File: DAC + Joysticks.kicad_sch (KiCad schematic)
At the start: 131 parts, among them J10 L Phono, J11 R Phono, J8 JOY0, J9 JOY1, U23 74HC374, U24 74HC374, U25 74HC244, U26 74HC244, U27 74HC373, U28 74HC244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

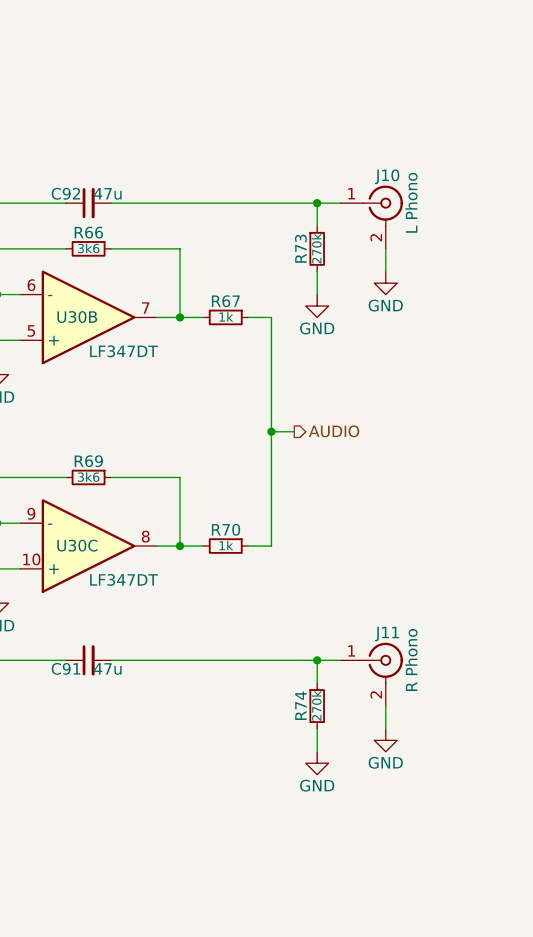
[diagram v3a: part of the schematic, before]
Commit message: motherboard: Added the main RCA-based audio out connections, completing the audio section
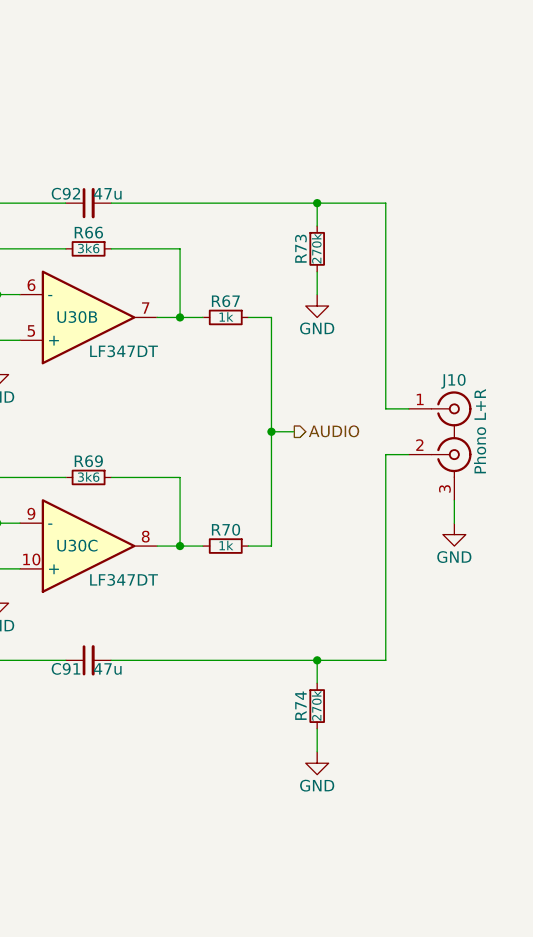
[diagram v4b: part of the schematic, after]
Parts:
- removed J10: L Phono, symbol Connector:Conn_Coaxial
- removed J11: R Phono, symbol Connector:Conn_Coaxial
- added J10: Phono L+R, rhais_connector-multicomp:PSG01550, symbol Connector:Conn_Coaxial_x2
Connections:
- net GND: now also J10.3 (EXT)
- net at C91.2, R74.1: now also J10.2 (IN2)
- net at C92.2, R73.1: now also J10.1 (IN1)
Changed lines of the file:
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@@
 	(wire
 		(pts
+			(xy 393.7 205.74) (xy 396.24 205.74)
+		)
+		(stroke
+			(width 0)
+			(type default)
+		)
+	)
+	(wire
+		(pts
 			(xy 228.6 55.88) (xy 241.3 55.88)
 		)
@@
 	(wire
 		(pts
-			(xy 388.62 177.8) (xy 386.08 177.8)
+			(xy 386.08 177.8) (xy 393.7 177.8)
 		)
 		(stroke
@@
 	(wire
 		(pts
-			(xy 393.7 233.68) (xy 393.7 236.22)
+			(xy 401.32 210.82) (xy 401.32 213.36)
 		)
 		(stroke
@@
 	(wire
 		(pts
-			(xy 393.7 182.88) (xy 393.7 185.42)
-		)
-		(stroke
-			(width 0)
-			(type default)
-		)
-	)
-	(wire
-		(pts
 			(xy 299.72 154.94) (xy 302.26 154.94)
 		)
@@
 	(wire
 		(pts
-			(xy 388.62 228.6) (xy 386.08 228.6)
+			(xy 386.08 228.6) (xy 393.7 228.6)
 		)
 		(stroke
@@
 	(wire
 		(pts
+			(xy 396.24 200.66) (xy 393.7 200.66)
+		)
+		(stroke
+			(width 0)
+			(type default)
+		)
+	)
+	(wire
+		(pts
 			(xy 325.12 142.24) (xy 320.04 142.24)
 		)
@@
 	(wire
 		(pts
+			(xy 393.7 228.6) (xy 393.7 205.74)
+		)
+		(stroke
+			(width 0)
+			(type default)
+		)
+	)
+	(wire
+		(pts
+			(xy 393.7 200.66) (xy 393.7 177.8)
+		)
+		(stroke
+			(width 0)
+			(type default)
+		)
+	)
+	(wire
+		(pts
 			(xy 40.64 81.28) (xy 104.14 81.28)
 		)
@@
 	)
 	(symbol
-		(lib_id "Connector:Conn_Coaxial")
-		(at 393.7 228.6 0)
-		(unit 1)
-		(exclude_from_sim no)
-		(in_bom yes)
-		(on_board yes)
-		(dnp no)
-		(property "Reference" "J11"
-			(at 393.954 225.552 0)
-			(effects
-				(font
-					(size 1.27 1.27)
-				)
-			)
-		)
-		(property "Value" "R Phono"
-			(at 396.621 228.6 90)
-			(effects
-				(font
-					(size 1.27 1.27)
-				)
-			)
-		)
-		(property "Footprint" ""
-			(at 393.7 228.6 0)
-			(effects
-				(font
-					(size 1.27 1.27)
-				)
-				(hide yes)
-			)
-		)
-		(property "Datasheet" "~"
-			(at 393.7 228.6 0)
-			(effects
-				(font
-					(size 1.27 1.27)
-				)
-				(hide yes)
-			)
-		)
-		(property "Description" "coaxial connector (BNC, SMA, SMB, SMC, Cinch/RCA, LEMO, ...)"
-			(at 393.7 228.6 0)
-			(effects
-				(font
-					(size 1.27 1.27)
-				)
-				(hide yes)
-			)
-		)
-		(pin "1"
-		)
-		(pin "2"
-		)
-		(instances
-			(project ""
-				(path "/6cc81c6b-09a2-4492-8ca2-d80a5c796e77/4fddf671-e1bf-4c63-ae08-e5f2b64aff0a"
-					(reference "J11")
-					(unit 1)
-				)
-			)
-		)
-	)
-	(symbol
 		(lib_id "power:GND")
 		(at 350.52 195.58 0)
@@
 	)
 	(symbol
+		(lib_id "Connector:Conn_Coaxial_x2")
+		(at 401.32 203.2 0)
+		(unit 1)
+		(exclude_from_sim no)
+		(in_bom yes)
+		(on_board yes)
+		(dnp no)
+		(property "Reference" "J10"
+			(at 401.32 197.485 0)
+			(effects
+				(font
+					(size 1.27 1.27)
+				)
+			)
+		)
+		(property "Value" "Phono L+R"
+			(at 404.241 203.2 90)
+			(effects
+				(font
+					(size 1.27 1.27)
+				)
+			)
+		)
+		(property "Footprint" "rhais_connector-multicomp:PSG01550"
+			(at 401.32 205.74 0)
+			(effects
+				(font
+					(size 1.27 1.27)
+				)
+				(hide yes)
+			)
+		)
+		(property "Datasheet" "http://www.farnell.com/datasheets/2826737.pdf"
+			(at 401.32 205.74 0)
+			(effects
+				(font
+					(size 1.27 1.27)
+				)
+				(hide yes)
+			)
+		)
+		(property "Description" "double coaxial connector (BNC, SMA, SMB, SMC, Cinch/RCA, LEMO, ...)"
+			(at 401.32 203.2 0)
+			(effects
+				(font
+					(size 1.27 1.27)
+				)
+				(hide yes)
+			)
+		)
+		(property "MFR" "Pro Signal"
+			(at 401.32 203.2 0)
+			(effects
+				(font
+					(size 1.27 1.27)
+				)
+				(hide yes)
+			)
+		)
+		(property "MPN" "PSG01550"
+			(at 401.32 203.2 0)
+			(effects
+				(font
+					(size 1.27 1.27)
+				)
+				(hide yes)
+			)
+		)
+		(property "OC_FARNELL" "1280669"
+			(at 401.32 203.2 0)
+			(effects
+				(font
+					(size 1.27 1.27)
+				)
+				(hide yes)
+			)
+		)
+		(pin "3"
+		)
+		(pin "2"
+		)
+		(pin "1"
+		)
+		(instances
+			(project ""
+				(path "/6cc81c6b-09a2-4492-8ca2-d80a5c796e77/4fddf671-e1bf-4c63-ae08-e5f2b64aff0a"
+					(reference "J10")
+					(unit 1)
+				)
+			)
+		)
+	)
+	(symbol
 		(lib_id "Device:Opamp_Quad")
 		(at 287.02 127 0)
@@
 	(symbol
 		(lib_id "power:GND")
-		(at 393.7 185.42 0)
-		(unit 1)
-		(exclude_from_sim no)
-		(in_bom yes)
-		(on_board yes)
-		(dnp no)
-		(property "Reference" "#PWR0193"
-			(at 393.7 191.77 0)
-			(effects
-				(font
-					(size 1.27 1.27)
-				)
-				(hide yes)
-			)
-		)
-		(property "Value" "GND"
-			(at 393.7 189.23 0)
-			(effects
-				(font
-					(size 1.27 1.27)
-				)
-			)
-		)
-		(property "Footprint" ""
-			(at 393.7 185.42 0)
-			(effects
-				(font
-					(size 1.27 1.27)
-				)
-				(hide yes)
-			)
-		)
-		(property "Datasheet" ""
-			(at 393.7 185.42 0)
-			(effects
-				(font
-					(size 1.27 1.27)
-				)
-				(hide yes)
-			)
-		)
-		(property "Description" "Power symbol creates a global label with name \"GND\" , ground"
-			(at 393.7 185.42 0)
-			(effects
-				(font
-					(size 1.27 1.27)
-				)
-				(hide yes)
-			)
-		)
-		(pin "1"
-		)
-		(instances
-			(project "dragonSTe"
-				(path "/6cc81c6b-09a2-4492-8ca2-d80a5c796e77/4fddf671-e1bf-4c63-ae08-e5f2b64aff0a"
-					(reference "#PWR0193")
-					(unit 1)
-				)
-			)
-		)
-	)
-	(symbol
-		(lib_id "power:GND")
-		(at 393.7 236.22 0)
+		(at 401.32 213.36 0)
 		(unit 1)
 		(exclude_from_sim no)
@@
 		(dnp no)
 		(property "Reference" "#PWR0192"
-			(at 393.7 242.57 0)
+			(at 401.32 219.71 0)
 			(effects
 				(font
@@
 		)
 		(property "Value" "GND"
-			(at 393.7 240.03 0)
+			(at 401.32 217.17 0)
 			(effects
 				(font
@@
 		)
 		(property "Footprint" ""
-			(at 393.7 236.22 0)
+			(at 401.32 213.36 0)
 			(effects
 				(font
@@
 		)
 		(property "Datasheet" ""
-			(at 393.7 236.22 0)
+			(at 401.32 213.36 0)
 			(effects
 				(font
@@
 		)
 		(property "Description" "Power symbol creates a global label with name \"GND\" , ground"
-			(at 393.7 236.22 0)
+			(at 401.32 213.36 0)
 			(effects
 				(font
@@
 					(unit 1)
 				)
-			)
-		)
-	)
-	(symbol
-		(lib_id "Connector:Conn_Coaxial")
-		(at 393.7 177.8 0)
-		(unit 1)
-		(exclude_from_sim no)
-		(in_bom yes)
-		(on_board yes)
-		(dnp no)
-		(property "Reference" "J10"
-			(at 393.954 174.752 0)
-			(effects
-				(font
-					(size 1.27 1.27)
-				)
-			)
-		)
-		(property "Value" "L Phono"
-			(at 396.621 177.8 90)
-			(effects
-				(font
-					(size 1.27 1.27)
-				)
-			)
-		)
-		(property "Footprint" ""
-			(at 393.7 177.8 0)
-			(effects
-				(font
-					(size 1.27 1.27)
-				)
-				(hide yes)
-			)
-		)
-		(property "Datasheet" "~"
-			(at 393.7 177.8 0)
-			(effects
-				(font
-					(size 1.27 1.27)
-				)
-				(hide yes)
-			)
-		)
-		(property "Description" "coaxial connector (BNC, SMA, SMB, SMC, Cinch/RCA, LEMO, ...)"
-			(at 393.7 177.8 0)
-			(effects
-				(font
-					(size 1.27 1.27)
-				)
-				(hide yes)
-			)
-		)
-		(pin "1"
-		)
-		(pin "2"
-		)
-		(instances
-			(project ""
-				(path "/6cc81c6b-09a2-4492-8ca2-d80a5c796e77/4fddf671-e1bf-4c63-ae08-e5f2b64aff0a"
-					(reference "J10")
-					(unit 1)
-				)

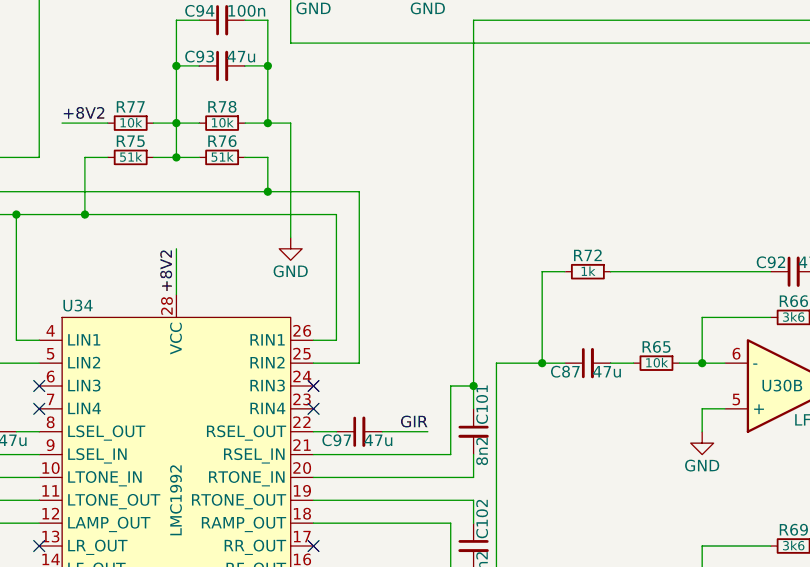
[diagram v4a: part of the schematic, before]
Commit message: motherboard: Added more footprints for parts and refined the serial comms section further
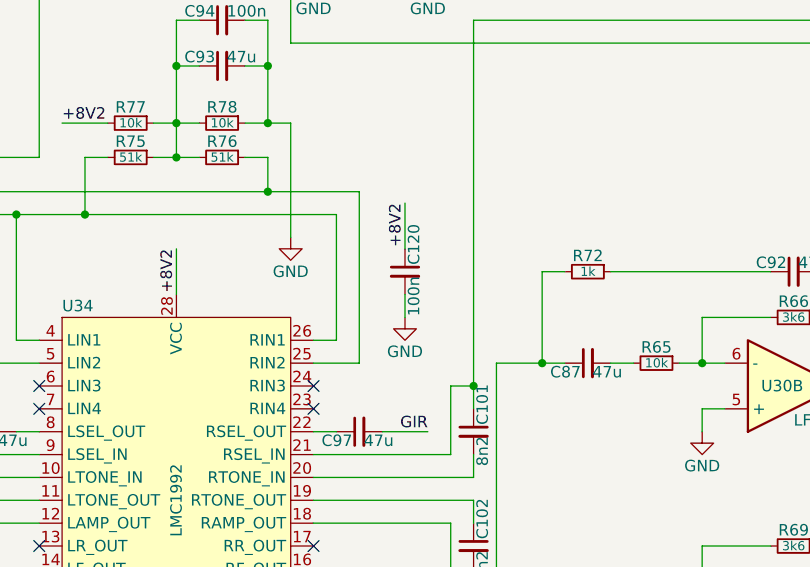
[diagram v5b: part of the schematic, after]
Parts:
- added C120: 100n, rhais_rcl:C0603, symbol Device:C_Small
- U34: MFR (none) -> Multicomp; MPN (none) -> SPC15504; OC_FARNELL (none) -> 2668410
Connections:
- net +8V2: now also C120.1
- net GND: now also C120.2
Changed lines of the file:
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@@
 	(wire
 		(pts
+			(xy 317.5 180.34) (xy 317.5 182.88)
+		)
+		(stroke
+			(width 0)
+			(type default)
+		)
+	)
+	(wire
+		(pts
 			(xy 109.22 68.58) (xy 106.68 68.58)
 		)
@@
 	(wire
 		(pts
+			(xy 317.5 170.18) (xy 317.5 175.26)
+		)
+		(stroke
+			(width 0)
+			(type default)
+		)
+	)
+	(wire
+		(pts
 			(xy 274.32 215.9) (xy 276.86 215.9)
 		)
@@
 		)
 	)
+	(label "+8V2"
+		(at 317.5 170.18 270)
+		(effects
+			(font
+				(size 1.27 1.27)
+			)
+			(justify right bottom)
+		)
+	)
 	(label "SysBus.D0"
 		(at 152.4 55.88 0)
@@
 			)
 		)
+		(property "MFR" "Multicomp"
+			(at 292.1 203.2 0)
+			(effects
+				(font
+					(size 1.27 1.27)
+				)
+				(hide yes)
+			)
+		)
+		(property "MPN" "SPC15504"
+			(at 292.1 203.2 0)
+			(effects
+				(font
+					(size 1.27 1.27)
+				)
+				(hide yes)
+			)
+		)
+		(property "OC_FARNELL" "2668410"
+			(at 292.1 203.2 0)
+			(effects
+				(font
+					(size 1.27 1.27)
+				)
+				(hide yes)
+			)
+		)
 		(pin "18"
 		)
@@
 	)
 	(symbol
+		(lib_id "power:GND")
+		(at 317.5 182.88 0)
+		(mirror y)
+		(unit 1)
+		(exclude_from_sim no)
+		(in_bom yes)
+		(on_board yes)
+		(dnp no)
+		(property "Reference" "#PWR0288"
+			(at 317.5 189.23 0)
+			(effects
+				(font
+					(size 1.27 1.27)
+				)
+				(hide yes)
+			)
+		)
+		(property "Value" "GND"
+			(at 317.5 186.69 0)
+			(effects
+				(font
+					(size 1.27 1.27)
+				)
+			)
+		)
+		(property "Footprint" ""
+			(at 317.5 182.88 0)
+			(effects
+				(font
+					(size 1.27 1.27)
+				)
+				(hide yes)
+			)
+		)
+		(property "Datasheet" ""
+			(at 317.5 182.88 0)
+			(effects
+				(font
+					(size 1.27 1.27)
+				)
+				(hide yes)
+			)
+		)
+		(property "Description" "Power symbol creates a global label with name \"GND\" , ground"
+			(at 317.5 182.88 0)
+			(effects
+				(font
+					(size 1.27 1.27)
+				)
+				(hide yes)
+			)
+		)
+		(pin "1"
+		)
+		(instances
+			(project "dragonSTe"
+				(path "/6cc81c6b-09a2-4492-8ca2-d80a5c796e77/4fddf671-e1bf-4c63-ae08-e5f2b64aff0a"
+					(reference "#PWR0288")
+					(unit 1)
+				)
+			)
+		)
+	)
+	(symbol
 		(lib_id "Device:C_Small")
 		(at 383.54 71.12 0)
@@
 					(unit 1)
 				)
+			)
+		)
+	)
+	(symbol
+		(lib_id "Device:C_Small")
+		(at 317.5 177.8 0)
+		(mirror y)
+		(unit 1)
+		(exclude_from_sim no)
+		(in_bom yes)
+		(on_board yes)
+		(dnp no)
+		(property "Reference" "C120"
+			(at 317.754 177.038 90)
+			(effects
+				(font
+					(size 1.27 1.27)
+				)
+				(justify left bottom)
+			)
+		)
+		(property "Value" "100n"
+			(at 317.754 178.308 90)
+			(effects
+				(font
+					(size 1.27 1.27)
+				)
+				(justify right bottom)
+			)
+		)
+		(property "Footprint" "rhais_rcl:C0603"
+			(at 317.5 177.8 0)
+			(effects
+				(font
+					(size 1.27 1.27)
+				)
+				(hide yes)
+			)
+		)
+		(property "Datasheet" "~"
+			(at 317.5 177.8 0)
+			(effects
+				(font
+					(size 1.27 1.27)
+				)
+				(hide yes)
+			)
+		)
+		(property "Description" "Unpolarized capacitor, small symbol"
+			(at 317.5 177.8 0)
+			(effects
+				(font
+					(size 1.27 1.27)
+				)
+				(hide yes)
+			)
+		)
+		(property "MFR" ""
+			(at 317.5 177.8 0)
+			(effects
+				(font
+					(size 1.27 1.27)
+				)
+				(hide yes)
+			)
+		)
+		(property "MPN" ""
+			(at 317.5 177.8 0)
+			(effects
+				(font
+					(size 1.27 1.27)
+				)
+				(hide yes)
+			)
+		)
+		(property "OC_FARNELL" ""
+			(at 317.5 177.8 0)
+			(effects
+				(font
+					(size 1.27 1.27)
+				)
+				(hide yes)
+			)
+		)
+		(pin "1"
+		)
+		(pin "2"
+		)
+		(instances
+			(project "dragonSTe"
+				(path "/6cc81c6b-09a2-4492-8ca2-d80a5c796e77/4fddf671-e1bf-4c63-ae08-e5f2b64aff0a"
+					(reference "C120")
+					(unit 1)
+				)

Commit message: motherboard: Sorted out the connectors for the joystick ports and video port
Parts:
- J8, J9: footprint Connector_Dsub:DSUB-15_Socket_Horizontal_P2.77x2.54mm_EdgePinOffset9.40mm -> Connector_Dsub:DSUB-15-HD_Socket_Horizontal_P2.29x2.54mm_EdgePinOffset8.35mm_Housed_MountingHolesOffset10.89mm; MFR (none) -> Amphenol; MPN (none) -> L77HDE15SD1CH4R; OC_DIGIKEY (none) -> 732-618015330923-ND; OC_FARNELL (none) -> 2401183
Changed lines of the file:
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@@
 			)
 		)
-		(property "Footprint" "Connector_Dsub:DSUB-15_Socket_Horizontal_P2.77x2.54mm_EdgePinOffset9.40mm"
+		(property "Footprint" "Connector_Dsub:DSUB-15-HD_Socket_Horizontal_P2.29x2.54mm_EdgePinOffset8.35mm_Housed_MountingHolesOffset10.89mm"
 			(at 39.37 53.34 0)
 			(effects
@@
 			)
 		)
-		(property "Datasheet" "~"
+		(property "Datasheet" "https://cdn.amphenol-cs.com/media/wysiwyg/files/drawing/l77hdxxxsd1ch4r.pdf"
 			(at 39.37 53.34 0)
 			(effects
@@
 			)
 		)
+		(property "MFR" "Amphenol"
+			(at 63.5 63.5 0)
+			(effects
+				(font
+					(size 1.27 1.27)
+				)
+				(hide yes)
+			)
+		)
+		(property "MPN" "L77HDE15SD1CH4R"
+			(at 63.5 63.5 0)
+			(effects
+				(font
+					(size 1.27 1.27)
+				)
+				(hide yes)
+			)
+		)
+		(property "OC_FARNELL" "2401183"
+			(at 63.5 63.5 0)
+			(effects
+				(font
+					(size 1.27 1.27)
+				)
+				(hide yes)
+			)
+		)
+		(property "OC_DIGIKEY" "732-618015330923-ND"
+			(at 63.5 63.5 0)
+			(effects
+				(font
+					(size 1.27 1.27)
+				)
+				(hide yes)
+			)
+		)
 		(pin "11"
 		)
@@
 			)
 		)
-		(property "Footprint" "Connector_Dsub:DSUB-15_Socket_Horizontal_P2.77x2.54mm_EdgePinOffset9.40mm"
+		(property "Footprint" "Connector_Dsub:DSUB-15-HD_Socket_Horizontal_P2.29x2.54mm_EdgePinOffset8.35mm_Housed_MountingHolesOffset10.89mm"
 			(at 39.37 129.54 0)
 			(effects
@@
 			)
 		)
-		(property "Datasheet" "~"
+		(property "Datasheet" "https://cdn.amphenol-cs.com/media/wysiwyg/files/drawing/l77hdxxxsd1ch4r.pdf"
 			(at 39.37 129.54 0)
 			(effects
@@
 			(at 63.5 139.7 0)
 			(effects
+				(font
+					(size 1.27 1.27)
+				)
+				(hide yes)
+			)
+		)
+		(property "MFR" "Amphenol"
+			(at 63.5 139.7 0)
+			(effects
+				(font
+					(size 1.27 1.27)
+				)
+				(hide yes)
+			)
+		)
+		(property "MPN" "L77HDE15SD1CH4R"
+			(at 63.5 139.7 0)
+			(effects
+				(font
+					(size 1.27 1.27)
+				)
+				(hide yes)
+			)
+		)
+		(property "OC_FARNELL" "2401183"
+			(at 63.5 139.7 0)
+			(effects
+				(font
+					(size 1.27 1.27)
+				)
+				(hide yes)
+			)
+		)
+		(property "OC_DIGIKEY" "732-618015330923-ND"
+			(at 63.5 139.7 0)
+			(effects

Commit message: motherboard: Routed the video output from SHIFTER
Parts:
- J8, J9: footprint Connector_Dsub:DSUB-15-HD_Socket_Horizontal_P2.29x2.54mm_EdgePinOffset8.35mm_Housed_MountingHolesOffset10.89mm -> rhais_connector-dsub:DSUB-15-HD_Socket_Horizontal_P2.29x2.54mm_EdgePinOffset8.35mm_Housed_MountingHolesOffset10.89mm
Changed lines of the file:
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@@
 			)
 		)
-		(property "Footprint" "Connector_Dsub:DSUB-15-HD_Socket_Horizontal_P2.29x2.54mm_EdgePinOffset8.35mm_Housed_MountingHolesOffset10.89mm"
+		(property "Footprint" "rhais_connector-dsub:DSUB-15-HD_Socket_Horizontal_P2.29x2.54mm_EdgePinOffset8.35mm_Housed_MountingHolesOffset10.89mm"
 			(at 39.37 53.34 0)
 			(effects
@@
 			)
 		)
-		(property "Footprint" "Connector_Dsub:DSUB-15-HD_Socket_Horizontal_P2.29x2.54mm_EdgePinOffset8.35mm_Housed_MountingHolesOffset10.89mm"
+		(property "Footprint" "rhais_connector-dsub:DSUB-15-HD_Socket_Horizontal_P2.29x2.54mm_EdgePinOffset8.35mm_Housed_MountingHolesOffset10.89mm"
 			(at 39.37 129.54 0)
 			(effects
